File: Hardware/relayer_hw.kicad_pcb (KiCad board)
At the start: 4 copper layers, 41 x 88.5 mm, 58 parts, among them J1 BOOT0, J2 AC_OUT, J3 STLink, J4 AC_IN, Q1 2N7002, SW1 NRST, SW2 USR_SW, U1 STM32WB55, U2 902-9040, U3 LM1117-3.3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

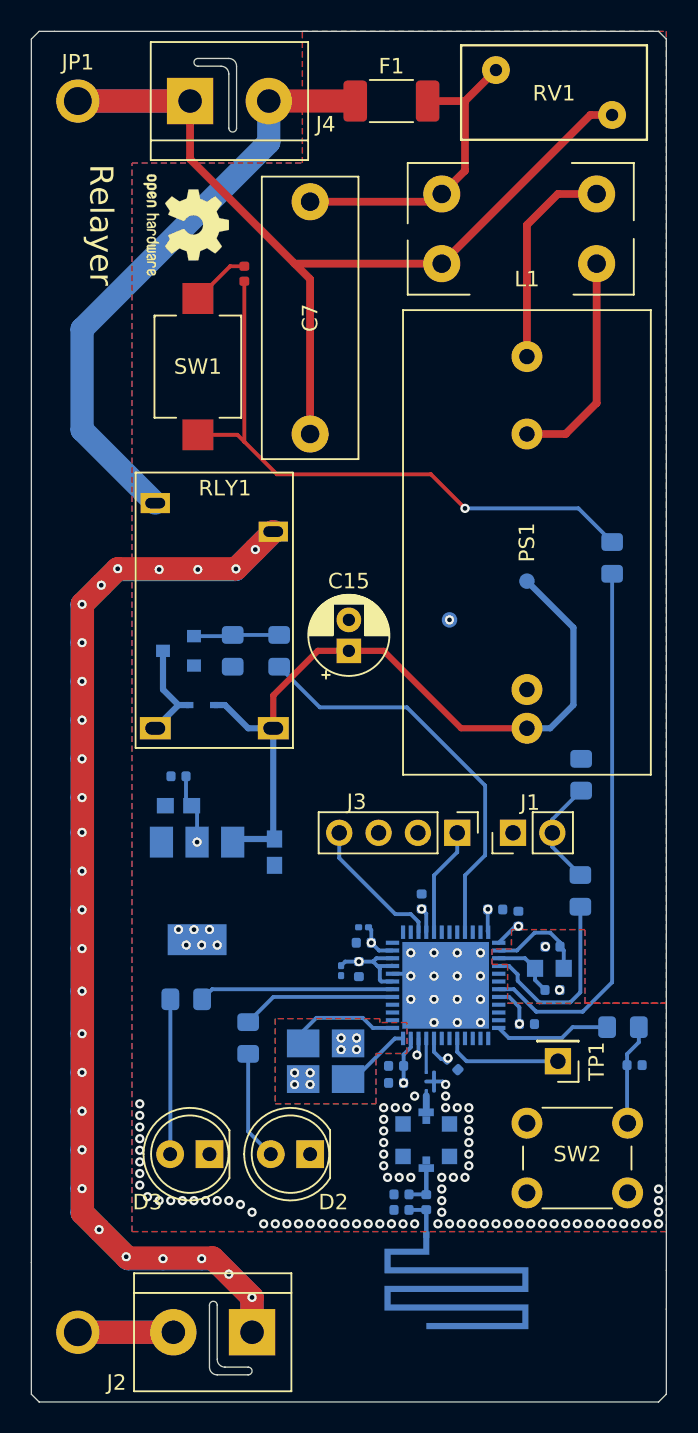
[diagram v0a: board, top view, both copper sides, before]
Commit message: Via stitching
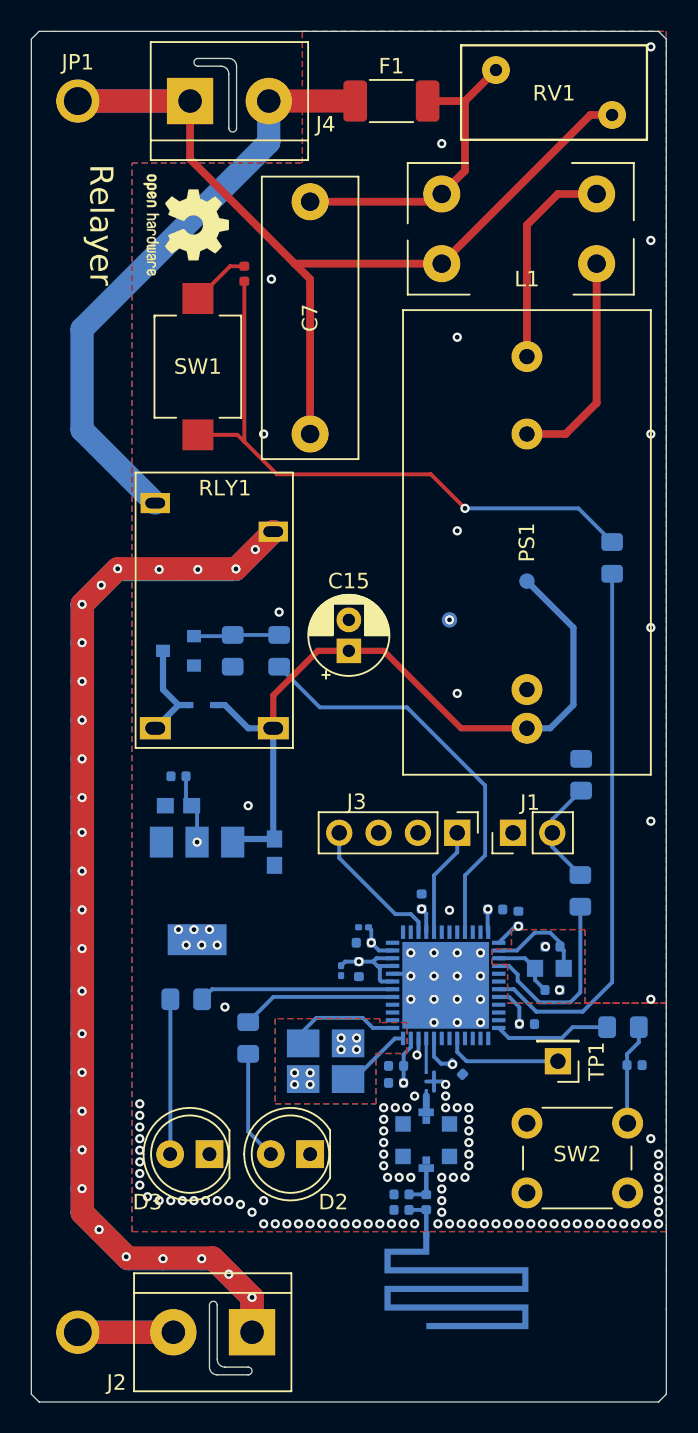
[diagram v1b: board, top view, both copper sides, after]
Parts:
- moved C10 0.42 mm to (158.5, 120.0)
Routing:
- net 3V3: track 26.8 -> 27.4 mm
- net GND: vias 109 -> 130
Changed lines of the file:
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@@
     (thickness 1.6)
     (drawings 29)
-    (tracks 403)
+    (tracks 424)
     (zones 0)
     (modules 58)
@@
   (page A4)
   (layers
-    (0 F.Cu signal hide)
+    (0 F.Cu signal)
     (1 VCC power hide)
-    (2 GND power hide)
+    (2 GND power)
     (31 B.Cu signal)
     (32 B.Adhes user)
@@
     (solder_mask_min_width 0.25)
     (aux_axis_origin 0 0)
+    (grid_origin 171 54)
     (visible_elements 7FFFFFFF)
     (pcbplotparams
@@
   )
   (module Capacitor_SMD:C_0402_1005Metric (layer B.Cu)
-    (at 158.2 119.7 315)
+    (at 158.5 120 315)
     (descr "Capacitor SMD 0402 (1005 Metric), square (rectangular) end terminal, IPC_7351 nominal, (Body size source: http://www.tortai-tech.com/upload/download/2011102023233369053.pdf), generated with kicad-footprint-generator")
     (tags capacitor)
@@
   (gr_line (start 172 53.5) (end 172 133) (layer Edge.Cuts) (width 0.05))
   (gr_line (start 132.5 53) (end 171.5 53) (layer Edge.Cuts) (width 0.05))
-  (segment (start 147.25 121.75) (end 146 121.75) (width 0.25) (layer GND) (net 50))
   (segment (start 165.375 112.34) (end 165.375 113.5) (width 0.25) (layer B.Cu) (net 1))
   (segment (start 165.135 112.1) (end 165.375 112.34) (width 0.25) (layer B.Cu) (net 1))
@@
   (segment (start 163.525 113.5) (end 162.875 112.85) (width 0.25) (layer B.Cu) (net 4))
   (via (at 158 91) (size 0.6) (drill 0.3) (layers F.Cu B.Cu) (net 5))
-  (via (at 157.9 119.3) (size 0.6) (drill 0.3) (layers F.Cu B.Cu) (net 5))
+  (via (at 158.2 119.7) (size 0.6) (drill 0.3) (layers F.Cu B.Cu) (net 5))
   (via (at 141 112) (size 0.6) (drill 0.3) (layers F.Cu B.Cu) (net 5))
   (via (at 142 112) (size 0.6) (drill 0.3) (layers F.Cu B.Cu) (net 5))
@@
   (segment (start 161.2 111.87) (end 161.18 111.85) (width 0.25) (layer B.Cu) (net 5))
   (segment (start 152.77 111.67) (end 152.95 111.85) (width 0.25) (layer B.Cu) (net 5))
-  (segment (start 157.857053 119.357053) (end 157.457053 119.357053) (width 0.25) (layer B.Cu) (net 5))
-  (segment (start 157 118.9) (end 157 118.03) (width 0.25) (layer B.Cu) (net 5))
-  (segment (start 157.457053 119.357053) (end 157 118.9) (width 0.25) (layer B.Cu) (net 5))
   (segment (start 151.265 113.065) (end 151 113.33) (width 0.25) (layer B.Cu) (net 5))
   (segment (start 152.15 113.065) (end 152.15 113.065) (width 0.25) (layer B.Cu) (net 5))
@@
   (segment (start 155.035 120.9) (end 155.035 119.8) (width 0.25) (layer B.Cu) (net 5))
   (via (at 155.035 120.9) (size 0.6) (drill 0.3) (layers F.Cu B.Cu) (net 5))
+  (segment (start 158.157053 119.657053) (end 157.457053 119.657053) (width 0.25) (layer B.Cu) (net 5))
+  (segment (start 157 119.2) (end 157 118.03) (width 0.25) (layer B.Cu) (net 5))
+  (segment (start 157.457053 119.657053) (end 157 119.2) (width 0.25) (layer B.Cu) (net 5))
   (segment (start 157.5 68) (end 148 68) (width 0.5) (layer F.Cu) (net 6))
   (segment (start 141.25 61.25) (end 141.25 57.5) (width 0.5) (layer F.Cu) (net 6))
   (segment (start 148 68) (end 141.25 61.25) (width 0.5) (layer F.Cu) (net 6))
-  (segment (start 149 69) (end 148 68) (width 0.5) (layer F.Cu) (net 6))
-  (segment (start 149 79) (end 149 69) (width 0.5) (layer F.Cu) (net 6))
   (segment (start 167.1 58.4) (end 157.5 68) (width 0.5) (layer F.Cu) (net 6))
   (segment (start 168.5 58.4) (end 167.1 58.4) (width 0.5) (layer F.Cu) (net 6))
@@
   (segment (start 134 137) (end 140.17 137) (width 1.5) (layer B.Cu) (net 6))
   (segment (start 134 57.5) (end 141.25 57.5) (width 1.5) (layer B.Cu) (net 6))
+  (segment (start 149 69) (end 148 68) (width 0.5) (layer F.Cu) (net 6))
+  (segment (start 149 79) (end 149 69) (width 0.5) (layer F.Cu) (net 6))
   (segment (start 163 98) (end 158.75 98) (width 0.4) (layer F.Cu) (net 7))
   (segment (start 153.75 93) (end 151.5 93) (width 0.4) (layer F.Cu) (net 7))
@@
   (segment (start 156.485 129.1) (end 156.5 129.085) (width 0.25) (layer B.Cu) (net 49))
   (segment (start 155.385 129.1) (end 156.485 129.1) (width 0.25) (layer B.Cu) (net 49))
+  (segment (start 147.25 121.75) (end 146 121.75) (width 0.25) (layer GND) (net 50))
   (via (at 152 118.75) (size 0.6) (drill 0.3) (layers F.Cu B.Cu) (net 50))
   (via (at 151 118.75) (size 0.6) (drill 0.3) (layers F.Cu B.Cu) (net 50))
@@
   (segment (start 154.32 113.85) (end 155.35 113.85) (width 0.25) (layer B.Cu) (net 50))
   (segment (start 165.1 114.9) (end 165.1 115.9) (width 0.25) (layer GND) (net 50))
+  (via (at 171.5 127) (size 0.6) (drill 0.3) (layers F.Cu B.Cu) (net 50))
+  (via (at 171.5 126.25) (size 0.6) (drill 0.3) (layers F.Cu B.Cu) (net 50))
+  (via (at 171.5 125.5) (size 0.6) (drill 0.3) (layers F.Cu B.Cu) (net 50))
+  (via (at 171 54) (size 0.6) (drill 0.3) (layers F.Cu B.Cu) (net 50))
+  (via (at 171 66.5) (size 0.6) (drill 0.3) (layers F.Cu B.Cu) (net 50))
+  (via (at 171 79) (size 0.6) (drill 0.3) (layers F.Cu B.Cu) (net 50))
+  (via (at 171 91.5) (size 0.6) (drill 0.3) (layers F.Cu B.Cu) (net 50))
+  (via (at 171 104) (size 0.6) (drill 0.3) (layers F.Cu B.Cu) (net 50))
+  (via (at 157.5 60.25) (size 0.6) (drill 0.3) (layers F.Cu B.Cu) (net 50))
+  (via (at 158.5 72.75) (size 0.6) (drill 0.3) (layers F.Cu B.Cu) (net 50))
+  (via (at 158.5 85.25) (size 0.6) (drill 0.3) (layers F.Cu B.Cu) (net 50))
+  (via (at 158.5 95.75) (size 0.6) (drill 0.3) (layers F.Cu B.Cu) (net 50))
+  (via (at 158 109.75) (size 0.6) (drill 0.3) (layers F.Cu B.Cu) (net 50))
+  (via (at 146 79) (size 0.6) (drill 0.3) (layers F.Cu B.Cu) (net 50))
+  (via (at 146 128.5) (size 0.6) (drill 0.3) (layers F.Cu B.Cu) (net 50))
+  (via (at 147 90.5) (size 0.6) (drill 0.3) (layers F.Cu B.Cu) (net 50))
+  (via (at 145 103) (size 0.6) (drill 0.3) (layers F.Cu B.Cu) (net 50))
+  (via (at 143.5 116) (size 0.6) (drill 0.3) (layers F.Cu B.Cu) (net 50))
+  (via (at 171 115.5) (size 0.6) (drill 0.3) (layers F.Cu B.Cu) (net 50))
+  (via (at 146.5 69) (size 0.6) (drill 0.3) (layers F.Cu B.Cu) (net 50))
+  (via (at 171 124.5) (size 0.6) (drill 0.3) (layers F.Cu B.Cu) (net 50))
   (segment (start 146.33 60.17) (end 134.27501 72.22499) (width 1.5) (layer B.Cu) (net 51))
   (segment (start 146.33 57.5) (end 146.33 60.17) (width 1.5) (layer B.Cu) (net 51))

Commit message: Correcao nos capacitores/Revisões de nets
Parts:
- C12, C5: footprint Capacitor_SMD:C_0201_0603Metric -> Capacitor_SMD:C_0402_1005Metric
- moved C5 0.20 mm to (152.4, 110.7)
- moved C12 0.11 mm to (150.9, 113.5)
- renumbered J1 to BOOT0, J3 to STLink
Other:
- outline, holes or cut-outs redrawn
- board text added: "3v3"
- board text added: "CLK"
- board text added: "GND"
- board text added: "RST"
- board text added: "SWDIO"

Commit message: Revisao para especificacoes da JLCPCB
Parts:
- removed the REF** at (141.0, 65.5)
- added REF**: OSHW-Logo2_9.8x8mm_SilkScreen, Symbol:OSHW-Logo2_9.8x8mm_SilkScreen, F.Cu at (139.7, 65.2)
- C15: footprint Capacitor_THT:CP_Radial_D5.0mm_P2.00mm -> Usr_pretty_lib:cap_elec
- moved C15 1.18 mm to (151.3, 91.8)
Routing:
- net N: vias 0 -> 2
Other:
- outline, holes or cut-outs redrawn
- board text added: "SWDCLK"
- board text removed: "CLK"

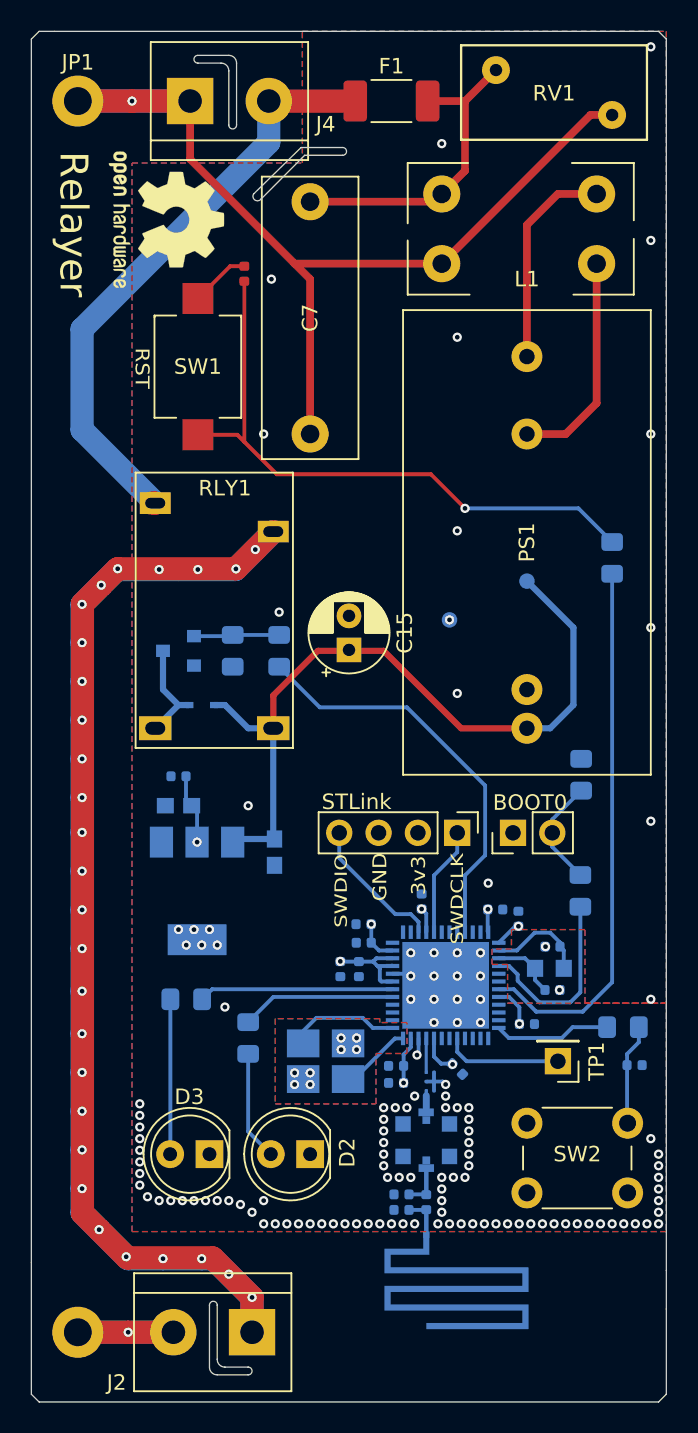
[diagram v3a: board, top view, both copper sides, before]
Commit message: Deixando a PCB soldavel
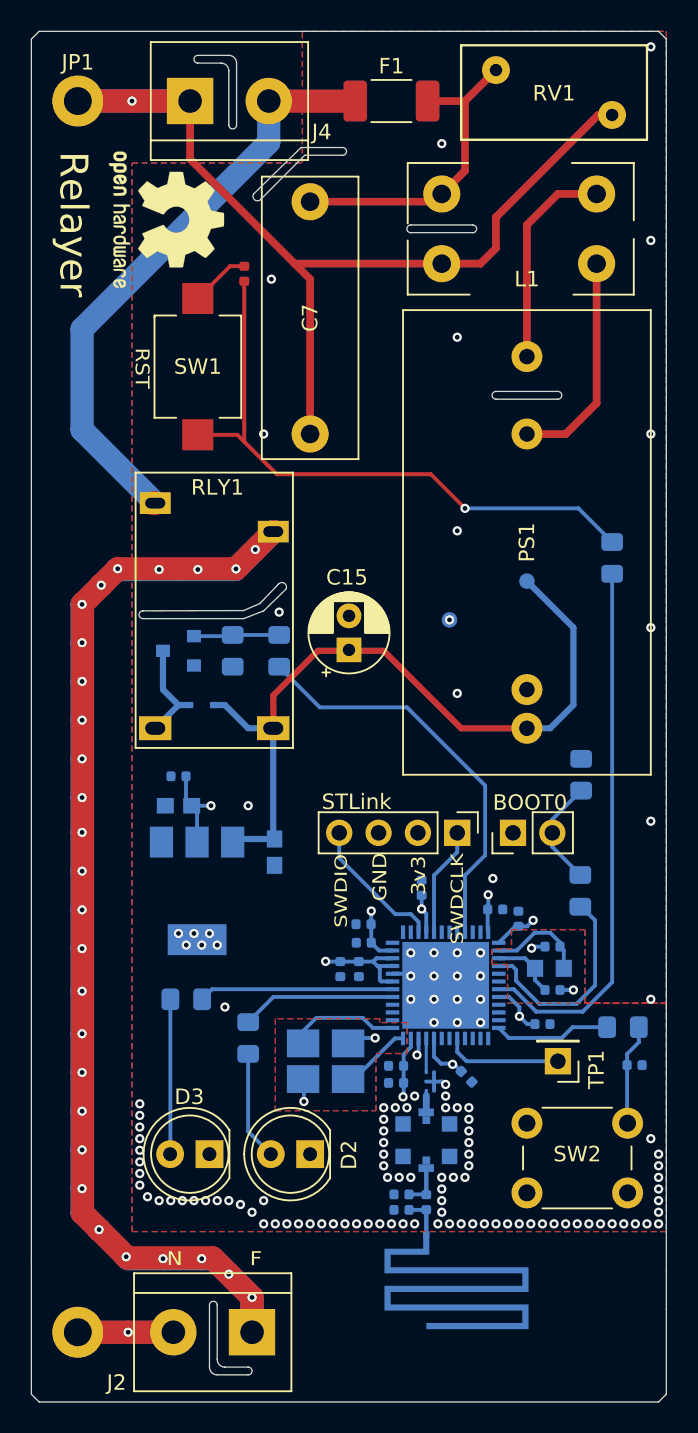
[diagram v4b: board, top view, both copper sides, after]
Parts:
- moved C9 1.00 mm to (164.0, 117.1)
- moved C13 0.89 mm to (156.2, 108.3)
- moved C10 0.78 mm to (159.1, 120.5)
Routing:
- net 3V3: track 27.5 -> 35.8 mm
- net GND: track 11.4 -> 16.5 mm, vias 130 -> 124
- net Net-(R2-Pad1): track 12.3 -> 13.7 mm
- net N: track 76.0 -> 77.2 mm
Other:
- outline, holes or cut-outs redrawn
- board text added: "F"
- board text added: "N"

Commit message: Segunda Revisão
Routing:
- net GND: track 16.5 -> 18.7 mm
- net Net-(J2-Pad1): vias 28 -> 27

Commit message: Aprimoramentos finais
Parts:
- moved C1 0.36 mm to (165.0, 112.1)
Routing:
- net 3V3: track 35.8 -> 34.6 mm, vias 16 -> 14
- net GND: track 18.7 -> 19.8 mm, vias 124 -> 215
